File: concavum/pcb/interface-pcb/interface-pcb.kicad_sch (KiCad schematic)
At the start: 9 parts, among them J1 Audio_Jack, J2 FPC_connector, U1 Adafruit_KB2040, U2 MCP23017/MCP23018

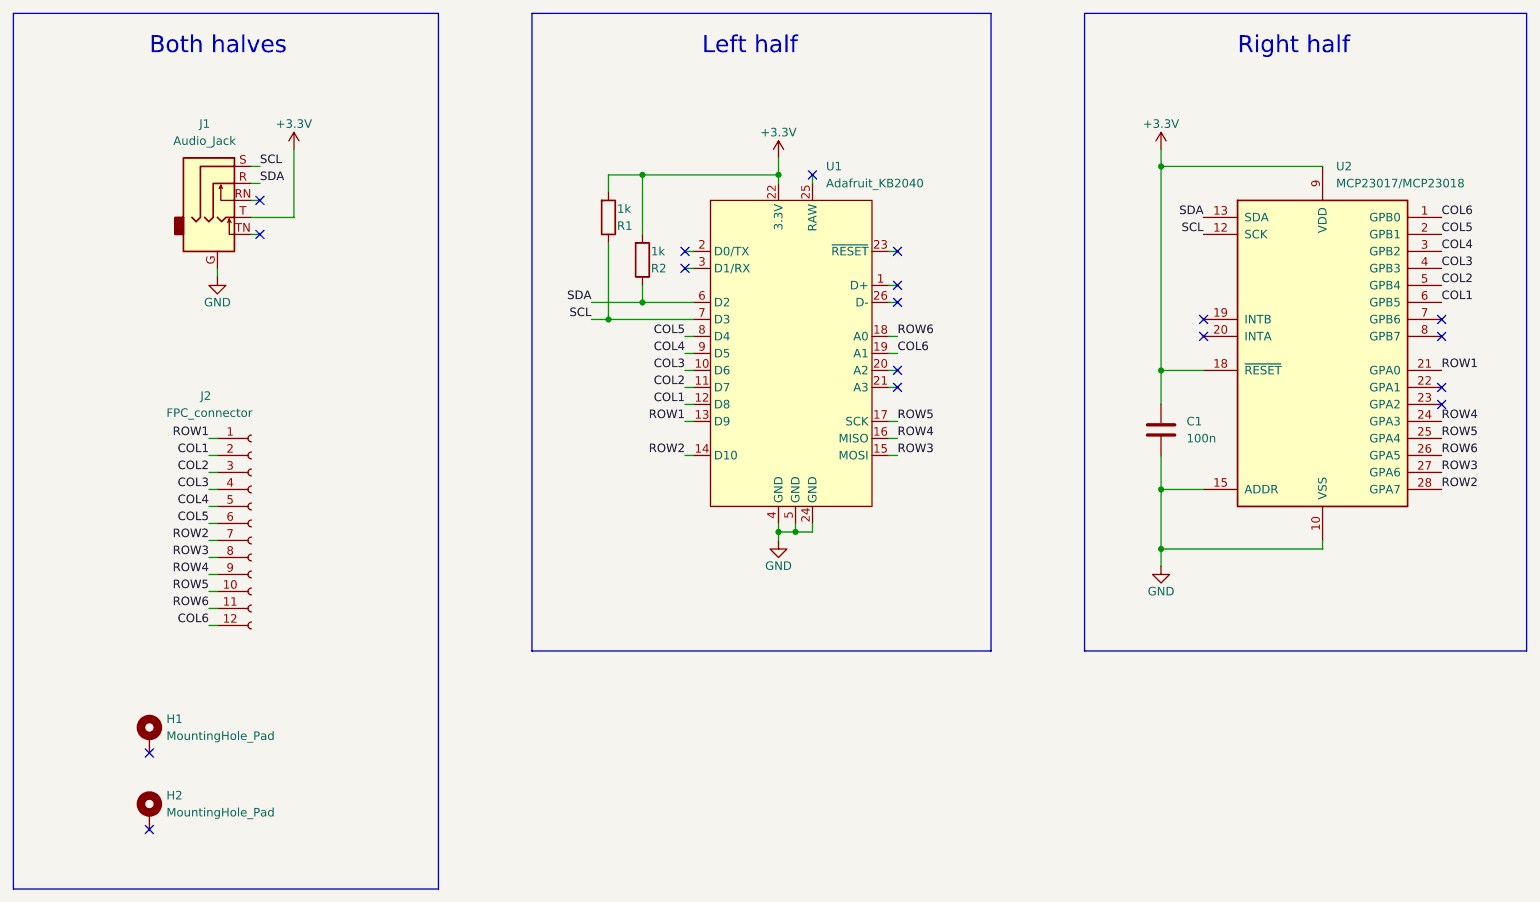
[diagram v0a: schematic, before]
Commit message: Update interface PCB files to KiCad 8 format
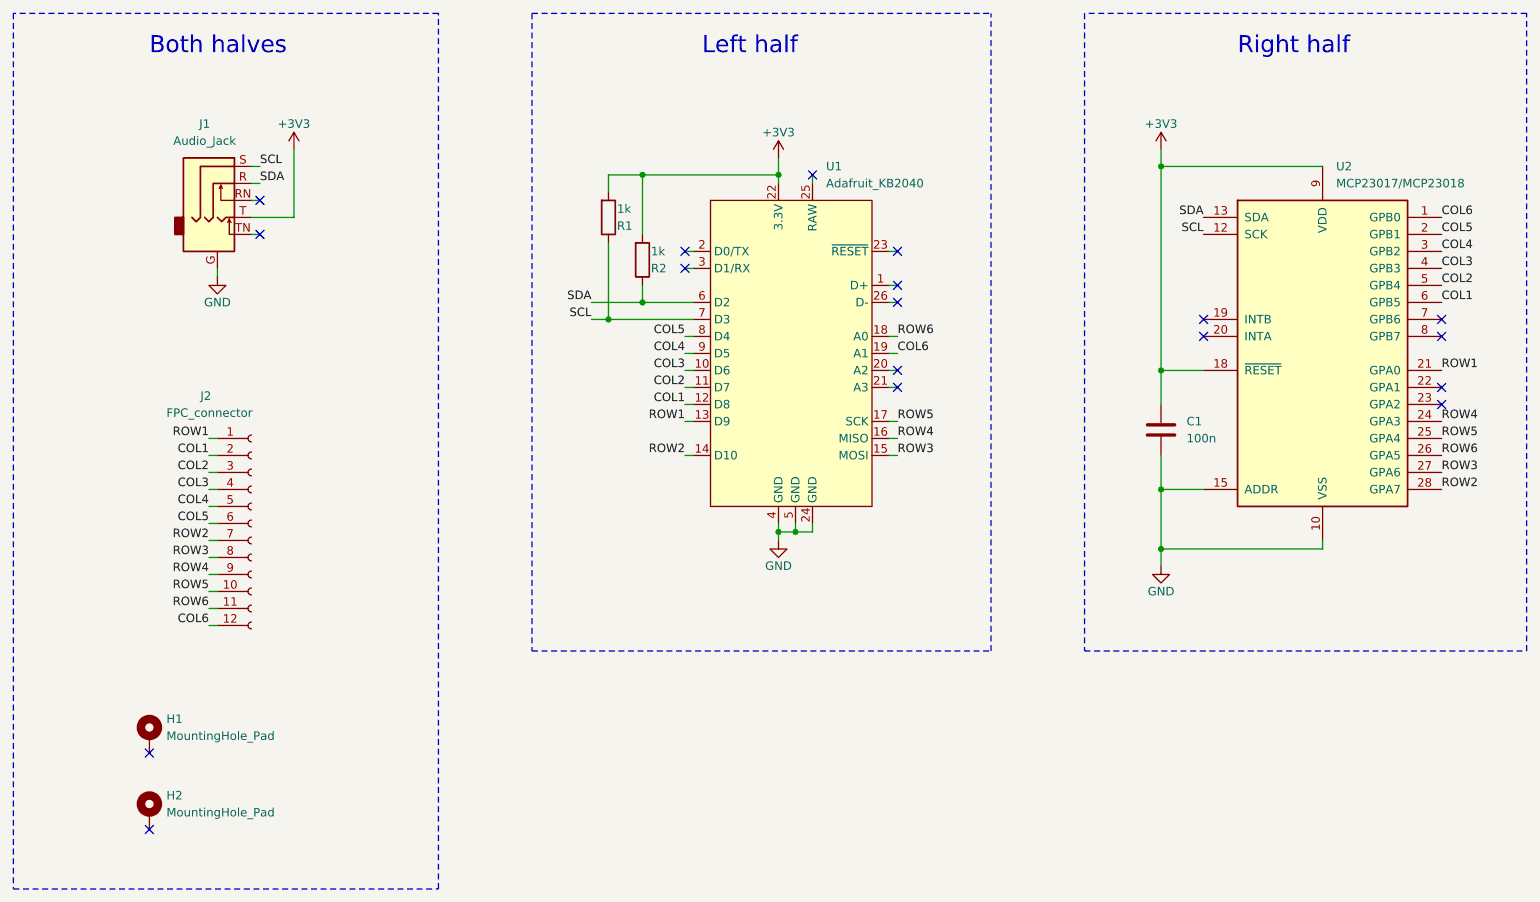
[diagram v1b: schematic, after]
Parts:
- U2: symbol Custom:MCP23017/MCP23018 -> Custom:MCP23017/MCP23018

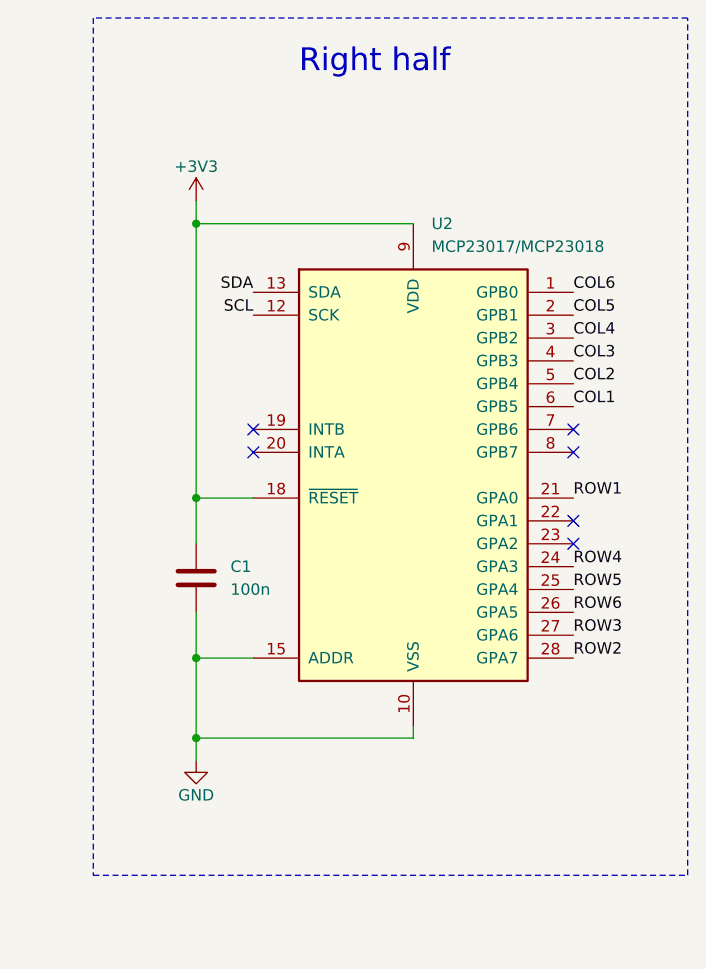
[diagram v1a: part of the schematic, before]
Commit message: Use the PCA9555 port expander for the right half
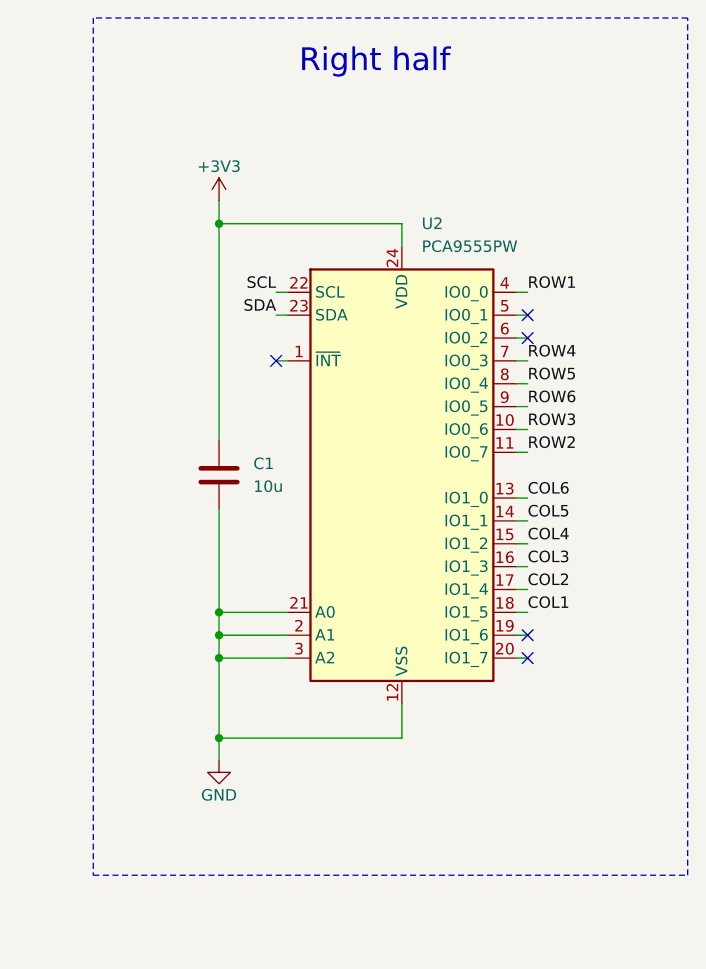
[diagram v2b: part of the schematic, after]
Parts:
- removed U2: MCP23017/MCP23018, Custom:MCP23017_SO_MCP23018_SO, symbol Custom:MCP23017/MCP23018
- added U2: PCA9555PW, Package_SO:TSSOP-24_4.4x7.8mm_P0.65mm, symbol Interface_Expansion:PCA9555PW
- C1: value 100n -> 10u
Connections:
- net +3V3: now also U2.24 (VDD)
- net COL1: now also U2.18 (IO1_5)
- net COL2: now also U2.17 (IO1_4)
- net COL3: now also U2.16 (IO1_3)
- net COL4: now also U2.15 (IO1_2)
- net COL5: now also U2.14 (IO1_1)
- net COL6: now also U2.13 (IO1_0)
- net GND: now also U2.12 (VSS), U2.2 (A1), U2.21 (A0), U2.3 (A2)
- net ROW1: now also U2.4 (IO0_0)
- net ROW2: now also U2.11 (IO0_7)
- net ROW3: now also U2.10 (IO0_6)
- net ROW4: now also U2.7 (IO0_3)
- net ROW5: now also U2.8 (IO0_4)
- net ROW6: now also U2.9 (IO0_5)
- net SCL: now also U2.22 (SCL)
- net SDA: now also U2.23 (SDA)
- no-connect marks 18 -> 17
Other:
- moved on the sheet: C1

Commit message: Change capacitor footprint to 0603
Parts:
- C1: footprint Capacitor_SMD:C_1206_3216Metric -> Capacitor_SMD:C_0603_1608Metric
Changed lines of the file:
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@@
 			)
 		)
-		(property "Footprint" "Capacitor_SMD:C_1206_3216Metric"
+		(property "Footprint" "Capacitor_SMD:C_0603_1608Metric"
 			(at 210.5152 93.98 0)
 			(effects
